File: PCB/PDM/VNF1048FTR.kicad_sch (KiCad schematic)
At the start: 17 parts, among them U4 VNF1048FTR

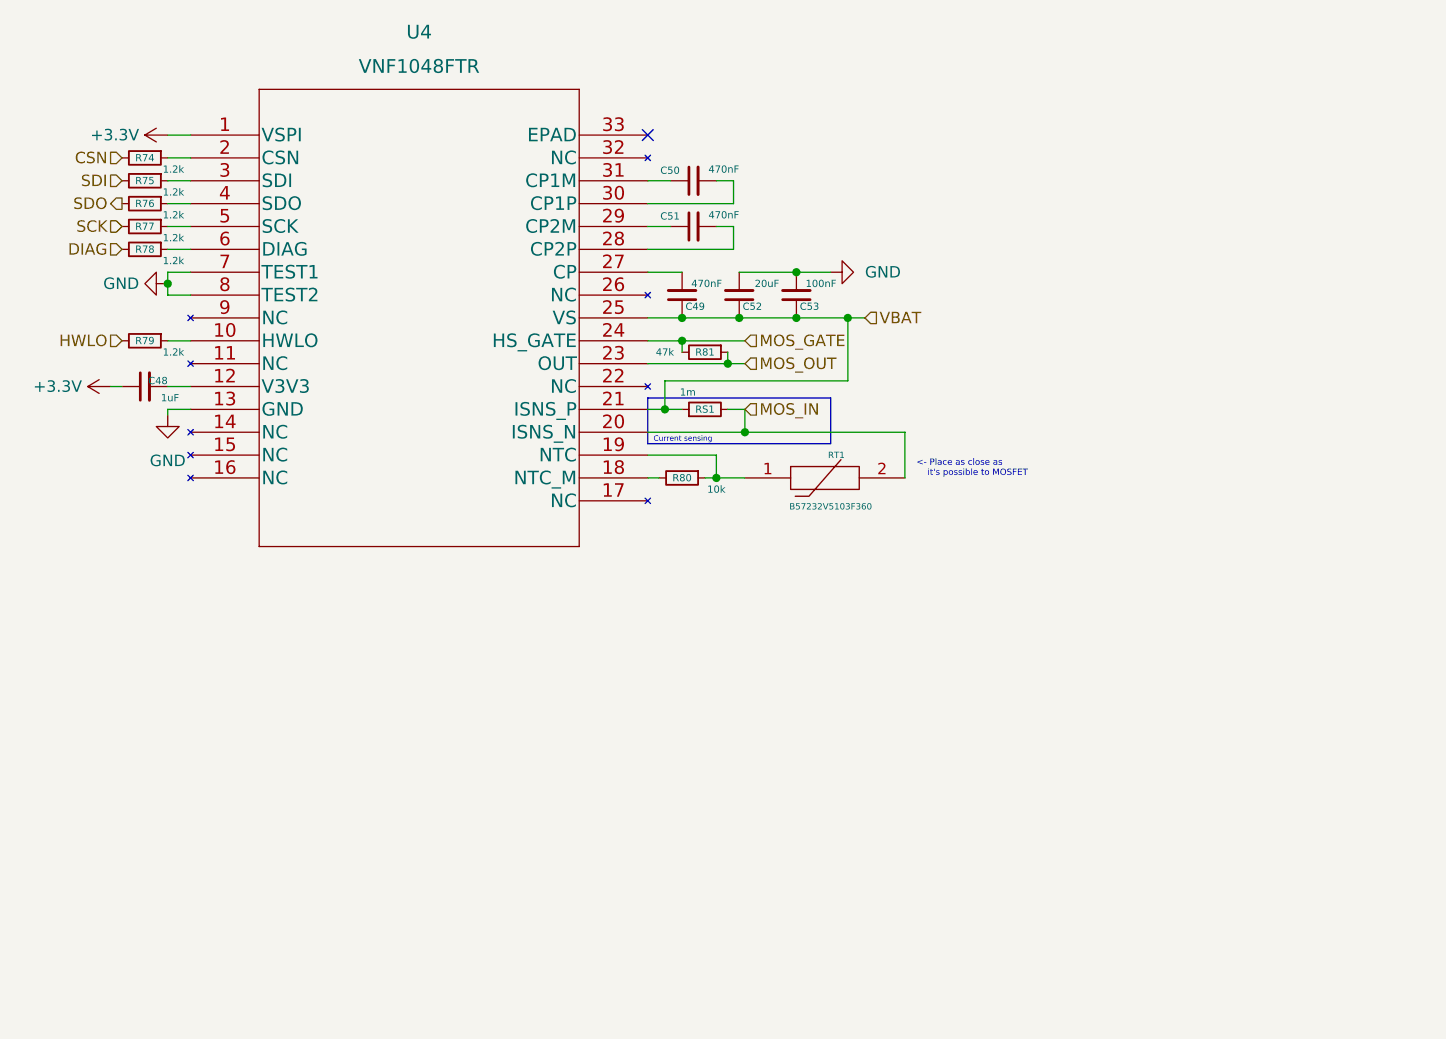
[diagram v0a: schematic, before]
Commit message: Added new type of high side driver based on VNF1048 + STL135
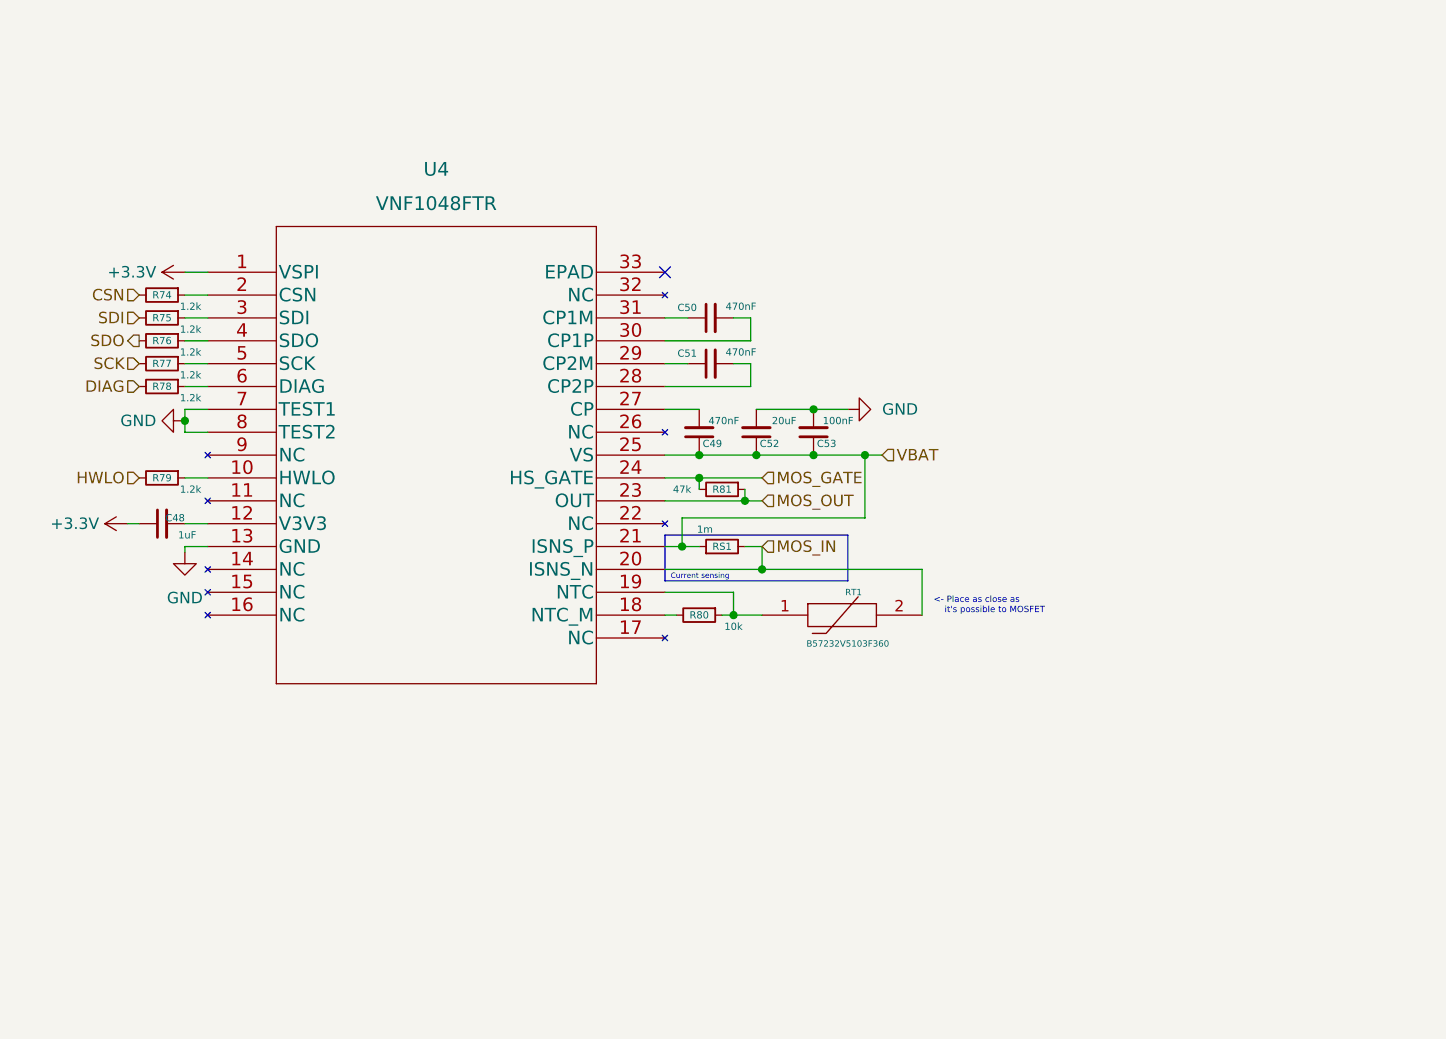
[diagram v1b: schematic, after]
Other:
- moved on the sheet: C48, C49, C50, C51, C52, C53, R74, R75, R76, R77, R78, R79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

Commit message: Finished high side section & fixed some ERC's errors
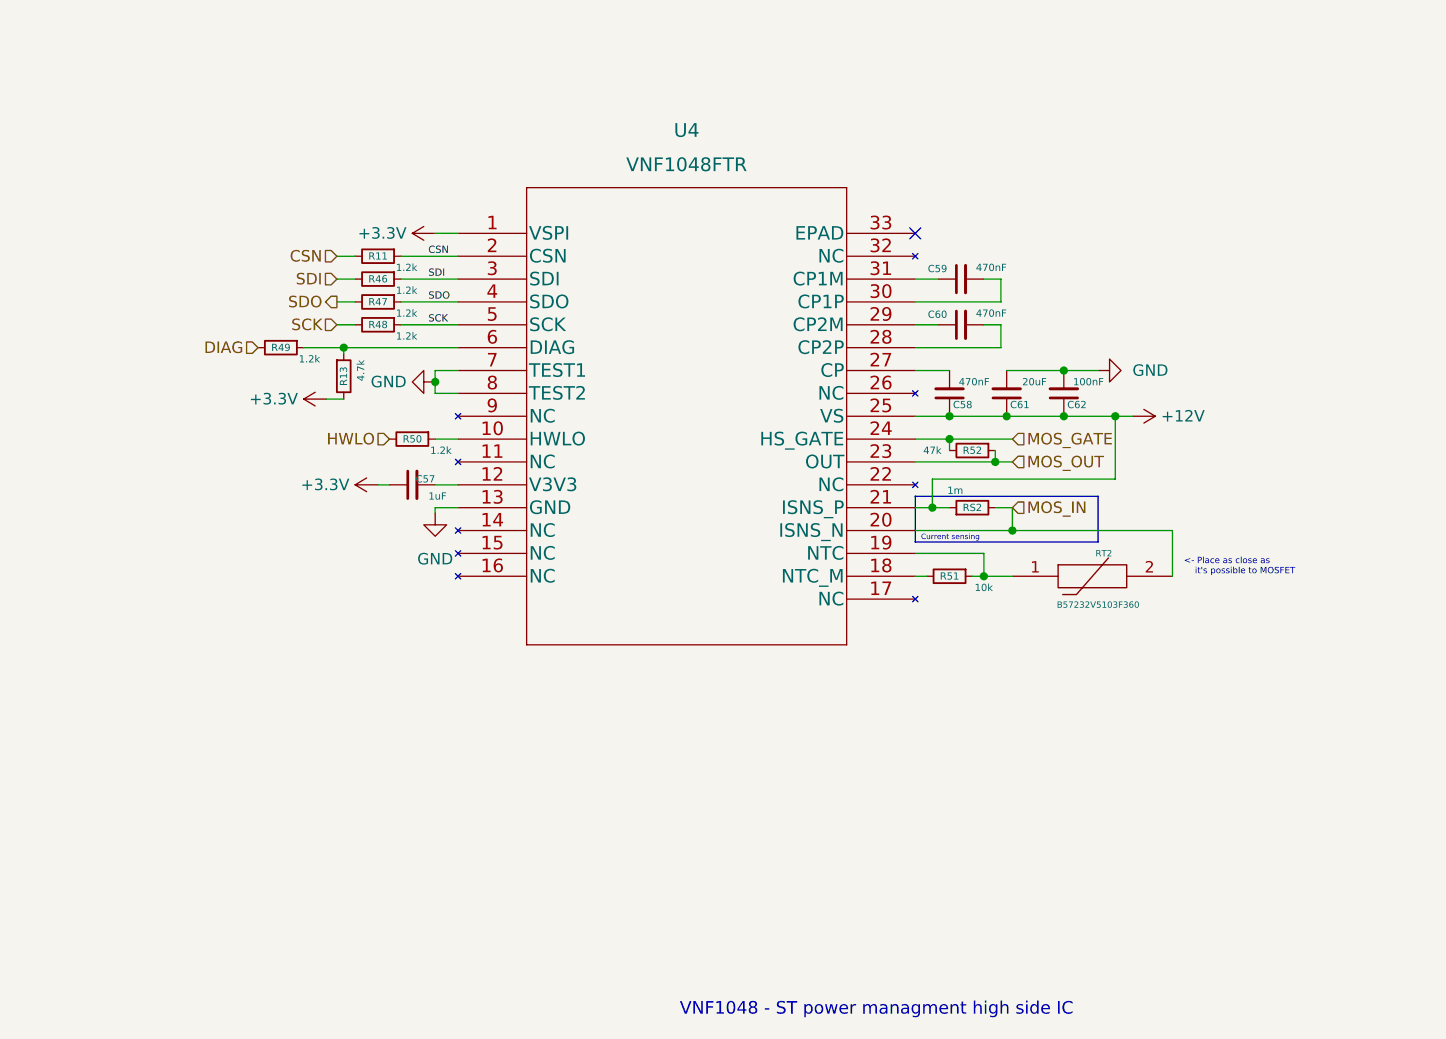
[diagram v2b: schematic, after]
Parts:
- added R13: 4.7k, Resistor_SMD:R_0402_1005Metric, symbol Device:R_Small
- renumbered C48 to C57, C49 to C58, C50 to C59, C51 to C60, C52 to C61, C53 to C62, R74 to R11, R75 to R46, R76 to R47, R77 to R48, R78 to R49, R79 to R50, R80 to R51, R81 to R52, RS1 to RS2, RT1 to RT2
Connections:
- net +3.3V: now also R13.2
- net CSN: now also R11.1, U4.2 (CSN)
- net SCK: now also R48.1, U4.5 (SCK)
- net SDI: now also R46.1, U4.3 (SDI)
- net SDO: now also R47.1, U4.4 (SDO)
- net at R49.1, U4.6 (DIAG): now also R13.1
- net VBAT renamed +12V
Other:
- note added: "VNF1048 - ST power managment high side IC"
- moved on the sheet: C57, C58, C59, C60, C61, C62, R11, R46, R47, R48, R49, R50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

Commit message: Minor changes in HS sechmatics
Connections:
- net +3.3V: no longer C57.1
- net GND: now also C57.1
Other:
- note added: "Internal LDO Output Capacitor as close as possible"
- moved on the sheet: C57, C58, C59, C60, C61, C62, R11, R13, R46, R47, R48, R49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

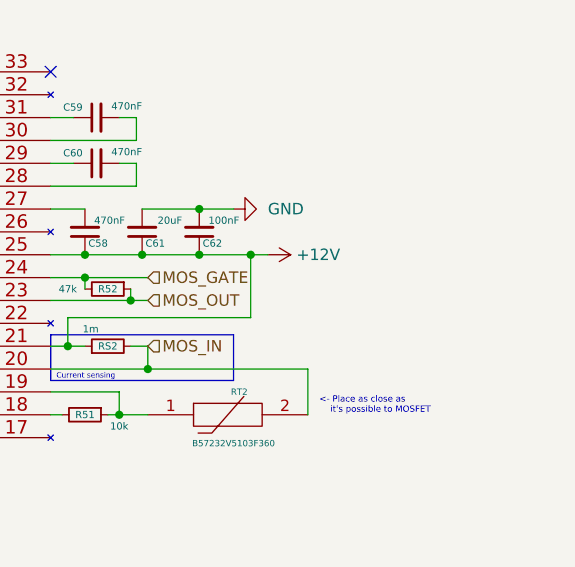
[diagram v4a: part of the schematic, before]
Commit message: Added fuse on each output of hs section - change footprint later!
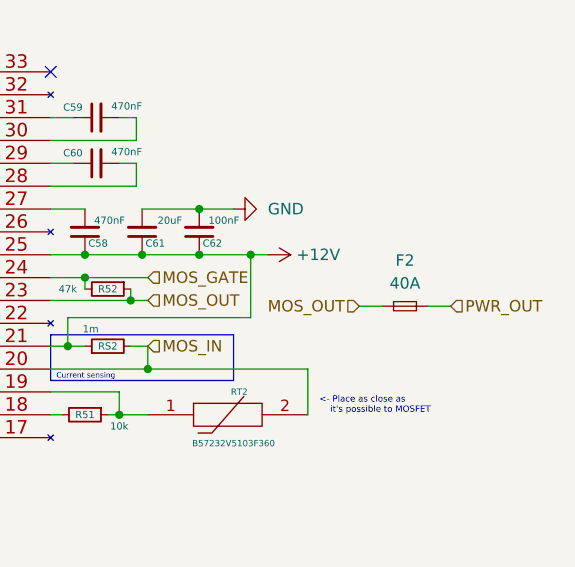
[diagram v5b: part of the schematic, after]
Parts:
- added F2: 40A, Fuse:Fuse_2512_6332Metric, symbol Device:Fuse_Small
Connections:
- net MOS_OUT: now also F2.1
- new net PWR_OUT: F2.2
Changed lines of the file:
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@@
+    (stroke (width 0) (type default) (color 0 0 0 0))
+  )
+  (wire (pts (xy 168.91 67.31) (xy 171.45 67.31))
     (stroke (width 0) (type default) (color 0 0 0 0))
   )
@@
   )
   (wire (pts (xy 128.905 68.58) (xy 128.905 71.755))
+    (stroke (width 0) (type default) (color 0 0 0 0))
+  )
+  (wire (pts (xy 161.29 67.31) (xy 163.83 67.31))
     (stroke (width 0) (type default) (color 0 0 0 0))
   )
@@
     (effects (font (size 0.8 0.8)) (justify left bottom))
   )
+  (hierarchical_label "MOS_OUT" (shape input) (at 161.29 67.31 180)
+    (effects (font (size 1.27 1.27)) (justify right))
+  )
   (hierarchical_label "SDI" (shape input) (at 62.738 46.355 180)
     (effects (font (size 1.27 1.27)) (justify right))
@@
   )
   (hierarchical_label "MOS_OUT" (shape input) (at 137.795 66.675 0)
+    (effects (font (size 1.27 1.27)) (justify left))
+  )
+  (hierarchical_label "PWR_OUT" (shape input) (at 171.45 67.31 0)
     (effects (font (size 1.27 1.27)) (justify left))
   )
@@
       (effects (font (size 1.27 1.27)) hide)
     )
+    (pin "1")
+    (pin "2")
+  )
+  (symbol (lib_id "Device:Fuse_Small") (at 166.37 67.31 0) (unit 1)
+    (in_bom yes) (on_board yes) (fields_autoplaced)
+    (property "Reference" "F2" (id 0) (at 166.37 62.23 0))
+    (property "Value" "40A" (id 1) (at 166.37 64.77 0))
+    (property "Footprint" "Fuse:Fuse_2512_6332Metric" (id 2) (at 166.37 67.31 0)
+      (effects (font (size 1.27 1.27)) hide)
+    )
+    (property "Datasheet" "~" (id 3) (at 166.37 67.31 0)
+      (effects (font (size 1.27 1.27)) hide)
+    )

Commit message: Added adc protection and HC header radsock
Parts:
- RS2: footprint Resistor_SMD:R_0402_1005Metric -> Resistor_SMD:R_2512_6332Metric
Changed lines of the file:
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@@
       (effects (font (size 0.8 0.8)))
     )
-    (property "Footprint" "Resistor_SMD:R_0402_1005Metric" (id 2) (at 133.35 71.755 0)
+    (property "Footprint" "Resistor_SMD:R_2512_6332Metric" (id 2) (at 133.35 71.755 0)
       (effects (font (size 1.27 1.27)) hide)
     )
